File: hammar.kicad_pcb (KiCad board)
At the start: 2 copper layers, 97.5 x 55 mm, 118 parts, among them J1 8x screw terminal, 5,08mm spa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, J10 1x2, J11 1x4, J12 1x3, J13 1x8, J14 1x3, J15 1x3, J16 1x3, J2 Micro_SD_Holder, J3 USB_C_Receptacle_USB2.0, J4 1x4, J5 1x4, J6 1x4, J7 1x4, J8 1x4, J9 1x2, Q1 S9014 or equivalent, Q2 S9014 or equivalent, Q3 TI CSD17310Q5A or equivalent, Q4 PMV40UN2R or equivalent, Q5 PMV40UN2R or equivalent, SW1 SW_MEC_5G, U1 A4988, U2 A4988, U3 A4988, U4 A4988, U5 DPAK 3,3v linear regulator + 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, U6 ESP32-WROOM-32E, U7 CH340G, Y1 Resonator_12mhz

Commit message: mix
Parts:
- renumbered J14 to X, J16 to Y, J15 to Z

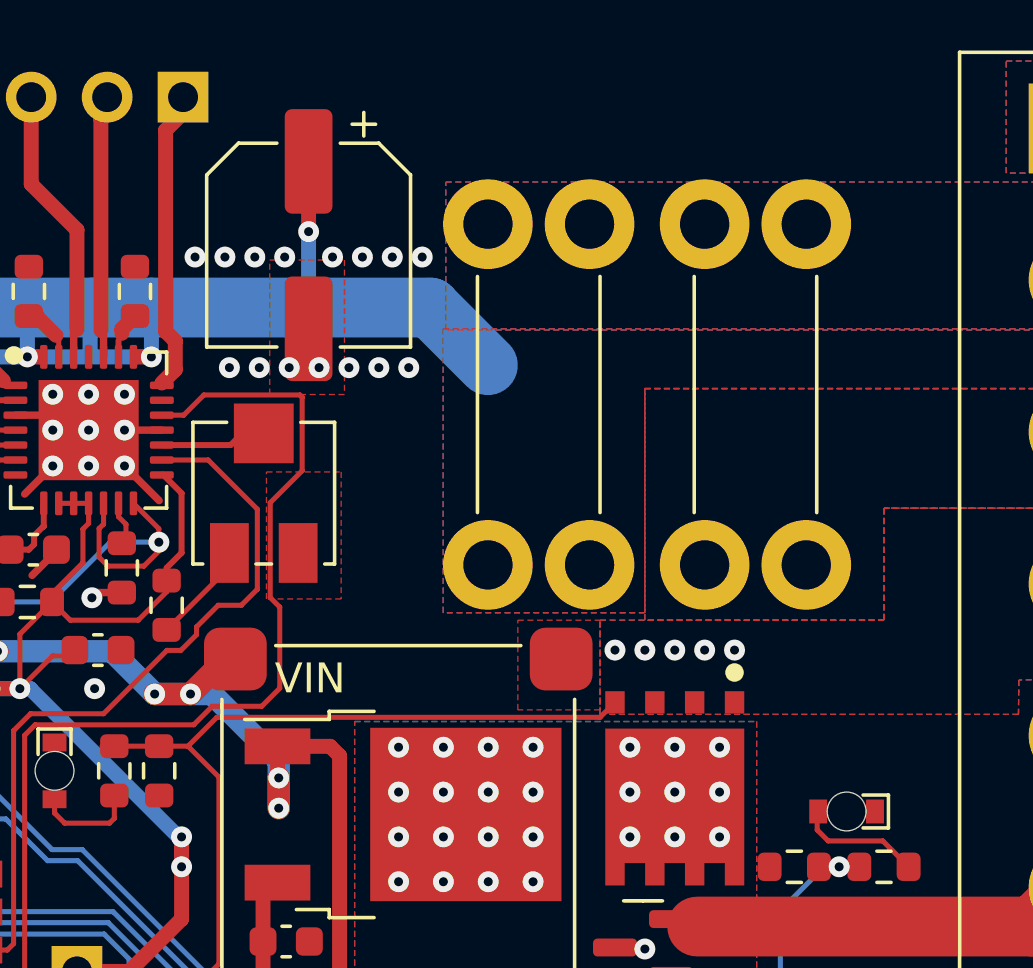
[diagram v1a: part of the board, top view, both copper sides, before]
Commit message: added 3D models
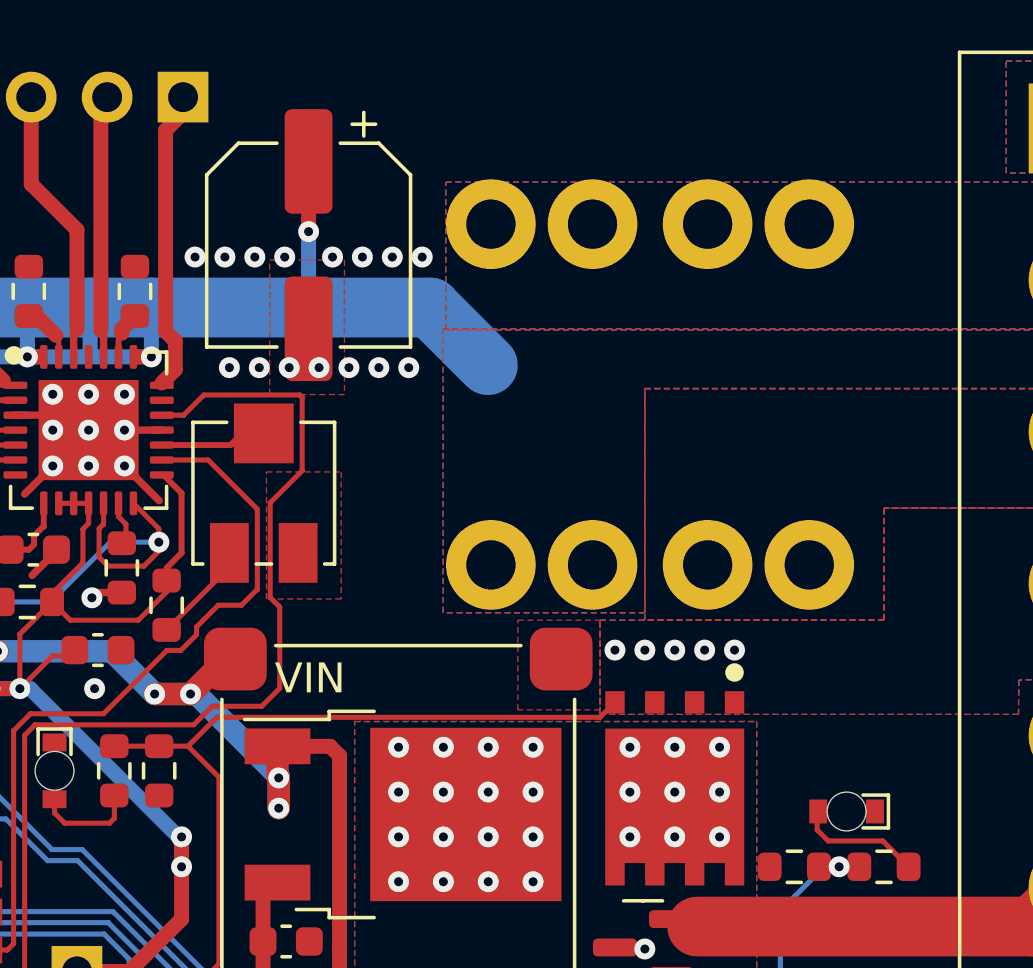
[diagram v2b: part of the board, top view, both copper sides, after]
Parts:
- F1, F2: moved to B.Cu
- moved G*** 0.30 mm to (138.9, 100.9)

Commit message: BOM++
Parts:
- R33: value 680Ω -> 10k
- moved D3 0.64 mm to (108.6, 100.4)
- moved R33 0.63 mm to (106.8, 100.3)
- renumbered X to J14, Z to J15, Y to J16
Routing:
- net Net-(J15-Pad3): track 19.3 -> 20.2 mm
- net Z-MIN: track 37.1 -> 37.6 mm
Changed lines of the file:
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@@
   )
   (footprint "Resistor_SMD:R_0603_1608Metric" (layer "F.Cu")
-    (at 106.805 100.972756 -90)
-    (descr "Resistor SMD 0603 (1608 Metric), square (rectangular) end terminal, IPC_7351 nominal, (Body size source: IPC-SM-782 page 72, https://www.pcb-3d.com/wordpress/wp-content/uploads/ipc-sm-782a_amendment_1_and_2.pdf), generated with kicad-footprint-generator")
-    (tags "resistor")
-    (property "Sheetfile" "File: hammar.kicad_sch")
-    (property "Sheetname" "")
-    (attr smd)
-    (fp_text reference "R33" (at 0 -1.43 90) (layer "F.SilkS") hide
-      (effects (font (size 1 1) (thickness 0.15)))
-    )
-    (fp_text value "680Ω" (at 0 1.43 90) (layer "F.Fab")
-      (effects (font (size 1 1) (thickness 0.15)))
-    )
-    (fp_text user "${REFERENCE}" (at 0 0 90) (layer "F.Fab")
-      (effects (font (size 0.4 0.4) (thickness 0.06)))
-    )
-    (fp_line (start -0.237258 -0.5225) (end 0.237258 -0.5225) (layer "F.SilkS") (width 0.12))
-    (fp_line (start -0.237258 0.5225) (end 0.237258 0.5225) (layer "F.SilkS") (width 0.12))
-    (fp_line (start -1.48 0.73) (end -1.48 -0.73) (layer "F.CrtYd") (width 0.05))
-    (fp_line (start 1.48 0.73) (end -1.48 0.73) (layer "F.CrtYd") (width 0.05))
-    (fp_line (start 1.48 -0.73) (end 1.48 0.73) (layer "F.CrtYd") (width 0.05))
-    (fp_line (start -1.48 -0.73) (end 1.48 -0.73) (layer "F.CrtYd") (width 0.05))
-    (fp_line (start -0.8 0.4125) (end -0.8 -0.4125) (layer "F.Fab") (width 0.1))
-    (fp_line (start 0.8 0.4125) (end -0.8 0.4125) (layer "F.Fab") (width 0.1))
-    (fp_line (start 0.8 -0.4125) (end 0.8 0.4125) (layer "F.Fab") (width 0.1))
-    (fp_line (start -0.8 -0.4125) (end 0.8 -0.4125) (layer "F.Fab") (width 0.1))
-    (pad "1" smd roundrect (at -0.825 0 270) (size 0.8 0.95) (layers "F.Cu" "F.Paste" "F.Mask") (roundrect_rratio 0.25)
-      (net 49 "Net-(J15-Pad3)") (pintype "passive"))
-    (pad "2" smd roundrect (at 0.825 0 270) (size 0.8 0.95) (layers "F.Cu" "F.Paste" "F.Mask") (roundrect_rratio 0.25)
-      (net 55 "Z-MIN") (pintype "passive"))
-    (model "${KICAD6_3DMODEL_DIR}/Resistor_SMD.3dshapes/R_0603_1608Metric.wrl"
-      (offset (xyz 0 0 0))
-      (scale (xyz 1 1 1))
-      (rotate (xyz 0 0 0))
-    )
-  )
-  (footprint "Resistor_SMD:R_0603_1608Metric" (layer "F.Cu")
     (at 131.605 76.972756 90)
     (descr "Resistor SMD 0603 (1608 Metric), square (rectangular) end terminal, IPC_7351 nominal, (Body size source: IPC-SM-782 page 72, https://www.pcb-3d.com/wordpress/wp-content/uploads/ipc-sm-782a_amendment_1_and_2.pdf), generated with kicad-footprint-generator")
@@
   )
   (footprint "Diode_SMD:D_SOD-323" (layer "F.Cu")
-    (at 108.555 101.012874 90)
+    (at 108.555 100.372874 90)
     (descr "SOD-323")
     (tags "SOD-323")
@@
     )
   )
+  (footprint "Resistor_SMD:R_0603_1608Metric" (layer "F.Cu")
+    (at 106.815 100.342756 -90)
+    (descr "Resistor SMD 0603 (1608 Metric), square (rectangular) end terminal, IPC_7351 nominal, (Body size source: IPC-SM-782 page 72, https://www.pcb-3d.com/wordpress/wp-content/uploads/ipc-sm-782a_amendment_1_and_2.pdf), generated with kicad-footprint-generator")
+    (tags "resistor")
+    (property "Sheetfile" "File: hammar.kicad_sch")
+    (property "Sheetname" "")
+    (attr smd)
+    (fp_text reference "R33" (at 0 -1.43 90) (layer "F.SilkS") hide
+      (effects (font (size 1 1) (thickness 0.15)))
+    )
+    (fp_text value "10k" (at 0 1.43 90) (layer "F.Fab")
+      (effects (font (size 1 1) (thickness 0.15)))
+    )
+    (fp_text user "${REFERENCE}" (at 0 0 90) (layer "F.Fab")
+      (effects (font (size 0.4 0.4) (thickness 0.06)))
+    )
+    (fp_line (start -0.237258 0.5225) (end 0.237258 0.5225) (layer "F.SilkS") (width 0.12))
+    (fp_line (start -0.237258 -0.5225) (end 0.237258 -0.5225) (layer "F.SilkS") (width 0.12))
+    (fp_line (start 1.48 0.73) (end -1.48 0.73) (layer "F.CrtYd") (width 0.05))
+    (fp_line (start -1.48 0.73) (end -1.48 -0.73) (layer "F.CrtYd") (width 0.05))
+    (fp_line (start 1.48 -0.73) (end 1.48 0.73) (layer "F.CrtYd") (width 0.05))
+    (fp_line (start -1.48 -0.73) (end 1.48 -0.73) (layer "F.CrtYd") (width 0.05))
+    (fp_line (start -0.8 -0.4125) (end 0.8 -0.4125) (layer "F.Fab") (width 0.1))
+    (fp_line (start 0.8 0.4125) (end -0.8 0.4125) (layer "F.Fab") (width 0.1))
+    (fp_line (start -0.8 0.4125) (end -0.8 -0.4125) (layer "F.Fab") (width 0.1))
+    (fp_line (start 0.8 -0.4125) (end 0.8 0.4125) (layer "F.Fab") (width 0.1))
+    (pad "1" smd roundrect (at -0.825 0 270) (size 0.8 0.95) (layers "F.Cu" "F.Paste" "F.Mask") (roundrect_rratio 0.25)
+      (net 49 "Net-(J15-Pad3)") (pintype "passive"))
+    (pad "2" smd roundrect (at 0.825 0 270) (size 0.8 0.95) (layers "F.Cu" "F.Paste" "F.Mask") (roundrect_rratio 0.25)
+      (net 55 "Z-MIN") (pintype "passive"))
+    (model "${KICAD6_3DMODEL_DIR}/Resistor_SMD.3dshapes/R_0603_1608Metric.wrl"
+      (offset (xyz 0 0 0))
+      (scale (xyz 1 1 1))
+      (rotate (xyz 0 0 0))
+    )
+  )
   (footprint "Package_TO_SOT_SMD:SOT-23" (layer "F.Cu")
     (at 133.715 92.222756)
@@
     (property "Sheetname" "")
     (attr through_hole)
-    (fp_text reference "Y" (at 0 2.33) (layer "B.SilkS")
+    (fp_text reference "J16" (at 0 2.33) (layer "B.SilkS")
       (effects (font (size 1.5 1.5) (thickness 0.3)) (justify mirror))
     )
@@
     (property "Sheetname" "")
     (attr through_hole)
-    (fp_text reference "X" (at 0 2.33) (layer "B.SilkS")
+    (fp_text reference "J14" (at 0 2.33) (layer "B.SilkS")
       (effects (font (size 1.5 1.5) (thickness 0.3)) (justify mirror))
     )
@@
     (property "Sheetname" "")
     (attr through_hole)
-    (fp_text reference "Z" (at 0 2.33 180) (layer "B.SilkS")
+    (fp_text reference "J15" (at 0 2.33 180) (layer "B.SilkS")
       (effects (font (size 1.5 1.5) (thickness 0.3)) (justify mirror))
     )
@@
   (segment (start 174.016176 113.452756) (end 176.036176 115.472756) (width 0.8) (layer "F.Cu") (net 48))
   (segment (start 179.305 116.687874) (end 179.305 115.722756) (width 0.25) (layer "F.Cu") (net 48))
-  (segment (start 106.045 100.907756) (end 106.045 102.907756) (width 0.17) (layer "F.Cu") (net 49))
-  (segment (start 106.045 102.907756) (end 104.555 104.397756) (width 0.17) (layer "F.Cu") (net 49))
-  (segment (start 104.555 104.397756) (end 104.555 115.212756) (width 0.17) (layer "F.Cu") (net 49))
+  (segment (start 106.815 99.517756) (end 106.24 99.517756) (width 0.17) (layer "F.Cu") (net 49))
   (segment (start 104.555 115.212756) (end 102.24 117.527756) (width 0.17) (layer "F.Cu") (net 49))
-  (segment (start 106.805 100.147756) (end 106.045 100.907756) (width 0.17) (layer "F.Cu") (net 49))
+  (segment (start 106.24 99.517756) (end 104.555 101.202756) (width 0.17) (layer "F.Cu") (net 49))
+  (segment (start 104.555 101.202756) (end 104.555 115.212756) (width 0.17) (layer "F.Cu") (net 49))
   (segment (start 132.6525 91.397756) (end 132.7775 91.272756) (width 0.17) (layer "F.Cu") (net 50))
   (segment (start 130.715 91.397756) (end 132.6525 91.397756) (width 0.17) (layer "F.Cu") (net 50))
@@
   (segment (start 99.55 119.137756) (end 97.965 117.552756) (width 0.17) (layer "F.Cu") (net 54))
   (segment (start 134.715 101.222756) (end 134.715 95.267756) (width 0.17) (layer "F.Cu") (net 55))
+  (segment (start 108.555 101.422874) (end 109.895118 101.422874) (width 0.17) (layer "F.Cu") (net 55))
+  (segment (start 108.555 101.422874) (end 107.070118 101.422874) (width 0.17) (layer "F.Cu") (net 55))
   (segment (start 134.715 95.267756) (end 134.765 95.217756) (width 0.17) (layer "F.Cu") (net 55))
-  (segment (start 116.315 101.972756) (end 116.665 102.322756) (width 0.17) (layer "F.Cu") (net 55))
-  (segment (start 106.805 101.797756) (end 106.98 101.972756) (width 0.17) (layer "F.Cu") (net 55))
-  (segment (start 106.98 101.972756) (end 116.315 101.972756) (width 0.17) (layer "F.Cu") (net 55))
+  (segment (start 107.070118 101.422874) (end 106.815 101.167756) (width 0.17) (layer "F.Cu") (net 55))
+  (segment (start 109.895118 101.422874) (end 111.120118 102.647874) (width 0.17) (layer "F.Cu") (net 55))
+  (segment (start 116.339882 102.647874) (end 116.665 102.322756) (width 0.17) (layer "F.Cu") (net 55))
+  (segment (start 111.120118 102.647874) (end 116.339882 102.647874) (width 0.17) (layer "F.Cu") (net 55))
   (segment (start 132.965 102.972756) (end 134.715 101.222756) (width 0.17) (layer "F.Cu") (net 55))
   (via (at 132.965 102.972756) (size 0.7) (drill 0.3) (layers "F.Cu" "B.Cu") (net 55))

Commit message: lil update
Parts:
- R1, R2, R3, R4, R5, R6, R7, R8: value 68mΩ -> 68mΩ shunt
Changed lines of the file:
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@@
       (effects (font (size 1 1) (thickness 0.15)))
     )
-    (fp_text value "68mΩ" (at 0 1.43) (layer "F.Fab")
+    (fp_text value "68mΩ shunt" (at 0 1.43) (layer "F.Fab")
       (effects (font (size 1 1) (thickness 0.15)))
     )
@@
       (effects (font (size 1 1) (thickness 0.15)))
     )
-    (fp_text value "68mΩ" (at 0 1.43 90) (layer "F.Fab")
+    (fp_text value "68mΩ shunt" (at 0 1.43 90) (layer "F.Fab")
       (effects (font (size 1 1) (thickness 0.15)))
     )
@@
       (effects (font (size 1 1) (thickness 0.15)))
     )
-    (fp_text value "68mΩ" (at 0 1.43 90) (layer "F.Fab")
+    (fp_text value "68mΩ shunt" (at 0 1.43 90) (layer "F.Fab")
       (effects (font (size 1 1) (thickness 0.15)))
     )
@@
       (effects (font (size 1 1) (thickness 0.15)))
     )
-    (fp_text value "68mΩ" (at 0 1.43 90) (layer "F.Fab")
+    (fp_text value "68mΩ shunt" (at 0 1.43 90) (layer "F.Fab")
       (effects (font (size 1 1) (thickness 0.15)))
     )
@@
       (effects (font (size 1 1) (thickness 0.15)))
     )
-    (fp_text value "68mΩ" (at 0 1.43 90) (layer "F.Fab")
+    (fp_text value "68mΩ shunt" (at 0 1.43 90) (layer "F.Fab")
       (effects (font (size 1 1) (thickness 0.15)))
     )
@@
       (effects (font (size 1 1) (thickness 0.15)))
     )
-    (fp_text value "68mΩ" (at 0 1.43 90) (layer "F.Fab")
+    (fp_text value "68mΩ shunt" (at 0 1.43 90) (layer "F.Fab")
       (effects (font (size 1 1) (thickness 0.15)))
     )
@@
       (effects (font (size 1 1) (thickness 0.15)))
     )
-    (fp_text value "68mΩ" (at 0 1.43 90) (layer "F.Fab")
+    (fp_text value "68mΩ shunt" (at 0 1.43 90) (layer "F.Fab")
       (effects (font (size 1 1) (thickness 0.15)))
     )
@@
       (effects (font (size 1 1) (thickness 0.15)))
     )
-    (fp_text value "68mΩ" (at 0 1.43) (layer "F.Fab")
+    (fp_text value "68mΩ shunt" (at 0 1.43) (layer "F.Fab")
       (effects (font (size 1 1) (thickness 0.15)))
     )

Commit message: fixed reference designators
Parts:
- moved G*** 1.70 mm to (138.9, 102.6)
- renumbered J14 to X, J16 to Y, J15 to Z
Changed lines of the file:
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@@
     (property "Sheetname" "")
     (attr through_hole)
-    (fp_text reference "J16" (at 0 2.33) (layer "B.SilkS")
+    (fp_text reference "Y" (at 0 2.33) (layer "B.SilkS")
       (effects (font (size 1.5 1.5) (thickness 0.3)) (justify mirror))
     )
@@
   )
   (footprint "LOGO" (layer "B.Cu")
-    (at 138.915 100.942756 -177)
+    (at 138.915 102.642756 -177)
     (attr board_only exclude_from_pos_files exclude_from_bom)
     (fp_text reference "G***" (at 0 0 3) (layer "B.SilkS") hide
@@
     (property "Sheetname" "")
     (attr through_hole)
-    (fp_text reference "J14" (at 0 2.33) (layer "B.SilkS")
+    (fp_text reference "X" (at 0 2.33) (layer "B.SilkS")
       (effects (font (size 1.5 1.5) (thickness 0.3)) (justify mirror))
     )
@@
     (property "Sheetname" "")
     (attr through_hole)
-    (fp_text reference "J15" (at 0 2.33 180) (layer "B.SilkS")
+    (fp_text reference "Z" (at 0 2.33 180) (layer "B.SilkS")
       (effects (font (size 1.5 1.5) (thickness 0.3)) (justify mirror))
     )
@@
     (effects (font (size 1 1) (thickness 0.15)) (justify mirror))
   )
-  (gr_text "Hammar\nv1,1" (at 138.655476 87.25) (layer "B.SilkS")
+  (gr_text "Hammar\nv1,1" (at 138.655476 88.95) (layer "B.SilkS")
     (effects (font (size 3 3) (thickness 0.5)) (justify mirror))
   )
